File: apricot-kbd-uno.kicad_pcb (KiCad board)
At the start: 2 copper layers, 65.4 x 58.4 mm, 6 parts, among them J101 Apricot Keyboard Port, J102 PS/2 Y, U101 TSR_1-2450, U102 MC1488, U103 MC1489

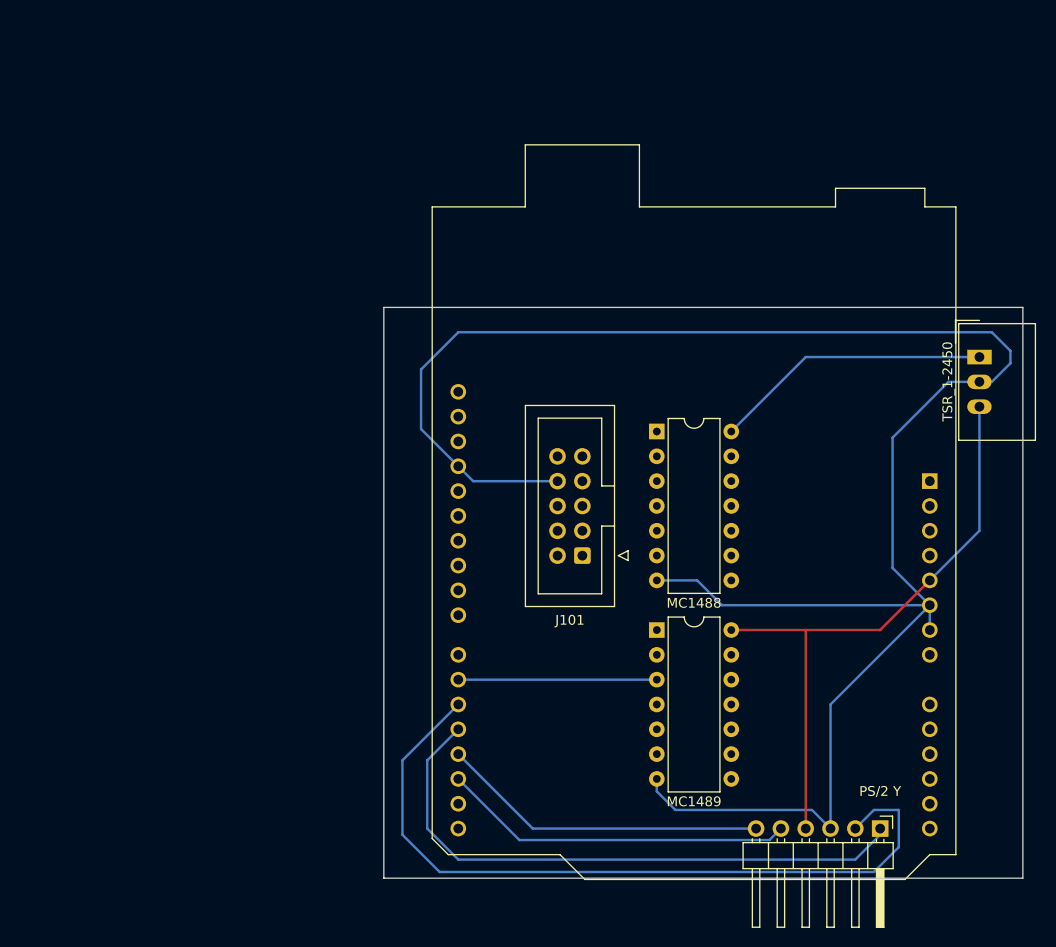
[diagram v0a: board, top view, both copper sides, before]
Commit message: assembly documentation. rev. uno-1.0
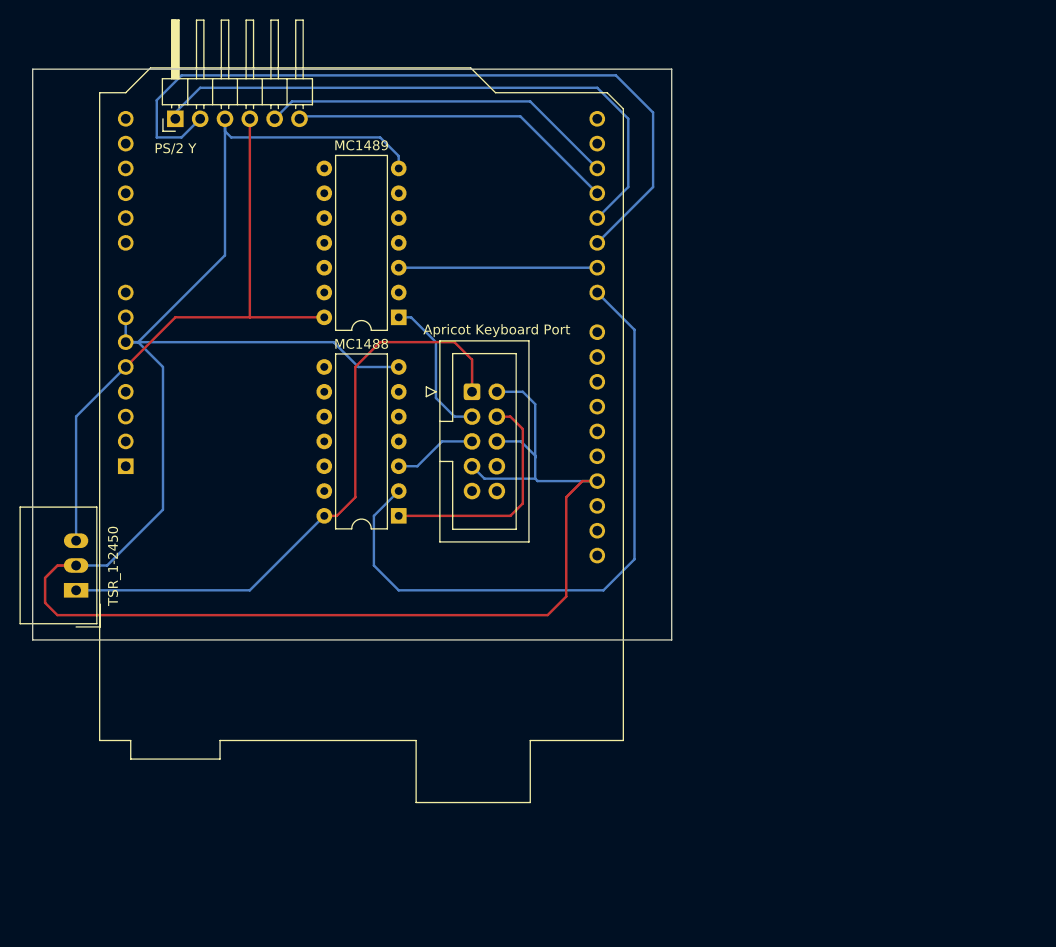
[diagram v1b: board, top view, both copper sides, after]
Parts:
- moved J102 102.4 mm to (90.4, 29.0), turned to 90 degrees
- moved U101 95.5 mm to (80.3, 77.2), turned to 90 degrees
- moved A101 82.3 mm to (85.3, 64.5), turned to 90 degrees
- moved U103 41.5 mm to (113.3, 49.3), turned to 180 degrees
- moved U102 27.8 mm to (113.3, 69.6), turned to 180 degrees
- moved J101 20.2 mm to (120.8, 56.9), turned to 0 degrees
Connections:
- A101 pad 29: GND -> EARTH
- A101 pad 6: GND -> EARTH
- A101 pad 7: GND -> EARTH
- J101 pad 2: RS232.OUT -> EARTH
- J101 pad 4: unconnected-(J101-Pad4) -> -12VDC
- J101 pad 5: unconnected-(J101-Pad5) -> RS232.OUT
- J101 pad 7: -12VDC -> EARTH
- J101 pad 8: GND -> unconnected-(J101-Pad8)
- J102 pad 3: GND -> EARTH
- U101 pad 2: GND -> EARTH
- U102 pad 7: GND -> EARTH
- U103 pad 7: GND -> EARTH
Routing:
- net EARTH: track 0.00 -> 215.6 mm
- net GND: track 199.4 -> 0.00 mm
- net UART.OUT: track 0.00 -> 66.6 mm
- net 12VDC: track 28.6 -> 62.9 mm
- net -12VDC: track 0.00 -> 24.0 mm
- net RS232.IN: track 0.00 -> 15.1 mm
- net RS232.OUT: track 0.00 -> 8.55 mm
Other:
- board text added: "-12V"
- board text added: "12V"
- board text added: "5V"
- board text added: "Back side: wiring only."
- board text added: "Front side: components only, towards Arduino"
- board text added: "GND"
- board text added: "KCLOCK"
- board text added: "KDATA"
- board text added: "RIN"
- board text added: "ROUT"
- board text added: "UIN"
- board text added: "UOUT"
